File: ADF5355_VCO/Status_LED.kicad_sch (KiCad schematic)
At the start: 9 parts, among them Q1 MMBT3904, Q2 MMBT3904, Q3 MMBT3904

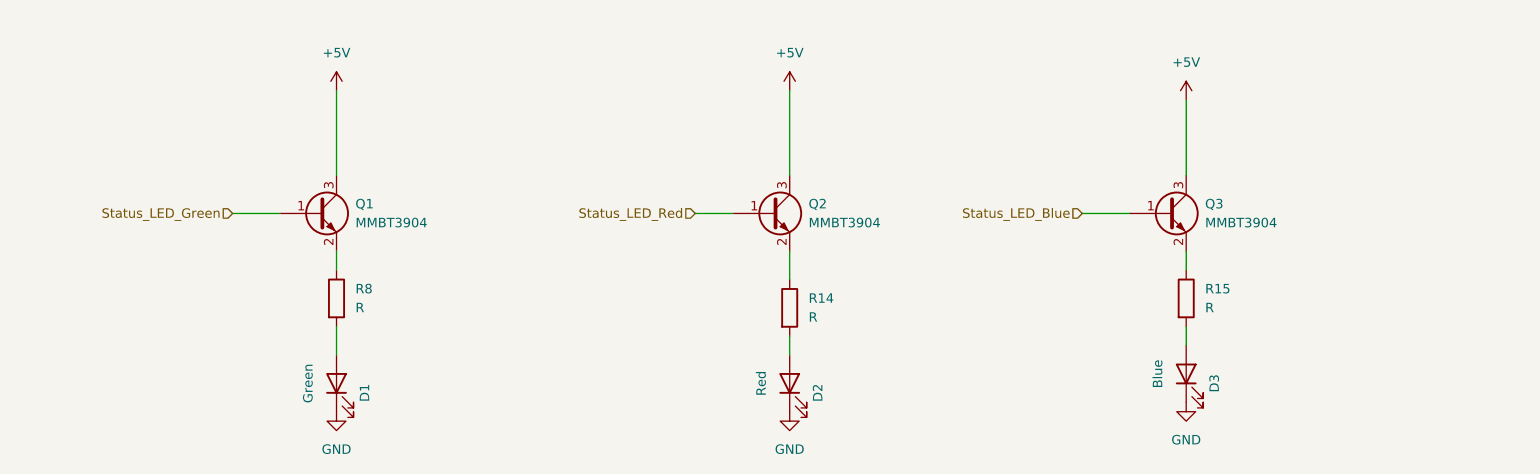
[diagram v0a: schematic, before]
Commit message: Added components for LED subsystem
Added resistor values and specific resistors and LEDs to BOM for the LED subsystem

Modified .gitignore to ignore autosave file
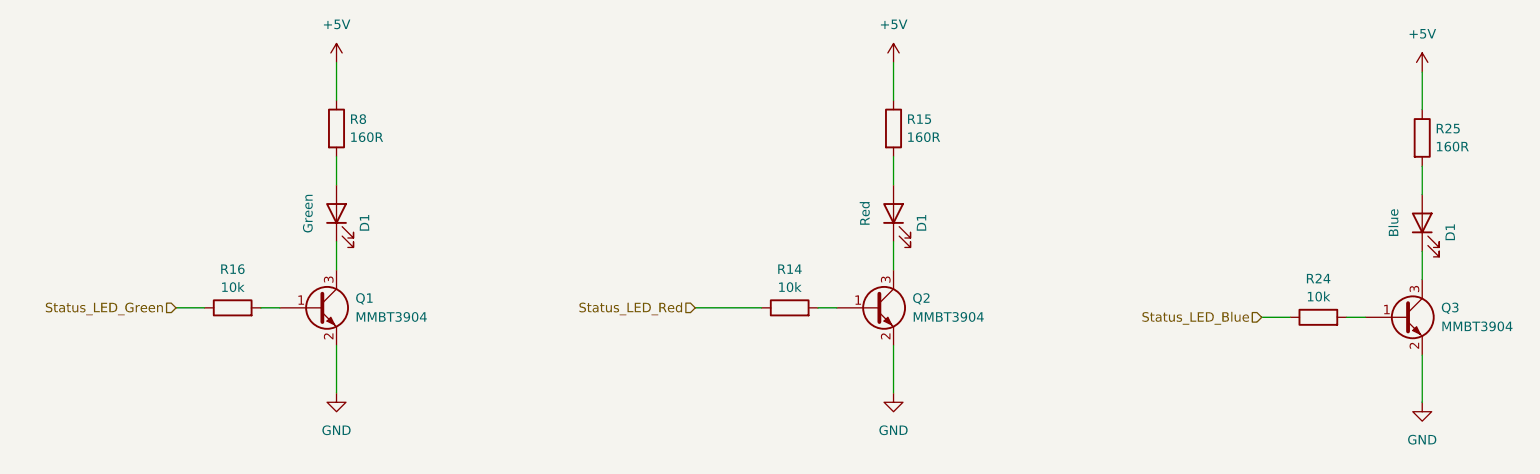
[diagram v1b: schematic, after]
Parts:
- removed D1: Green, symbol Device:LED
- removed D2: Red, symbol Device:LED
- removed D3: Blue, symbol Device:LED
- added D1: Red, LED_THT:LED_D4.0mm, symbol Device:LED
- added D1: Green, LED_THT:LED_D4.0mm, symbol Device:LED
- added D1: Blue, LED_THT:LED_D4.0mm, symbol Device:LED
- added R16, R24: 10k, Resistor_SMD:R_0603_1608Metric_Pad0.98x0.95mm_HandSolder, symbol Device:R
- added R25: 160R, Resistor_SMD:R_0603_1608Metric_Pad0.98x0.95mm_HandSolder, symbol Device:R
- R14: value R -> 10k; footprint (none) -> Resistor_SMD:R_0603_1608Metric_Pad0.98x0.95mm_HandSolder
- R15, R8: value R -> 160R; footprint (none) -> Resistor_SMD:R_0603_1608Metric_Pad0.98x0.95mm_HandSolder
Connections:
- net +5V: now also R15.1, R8.1, R25.1; no longer Q1.3 (C), Q2.3 (C), Q3.3 (C)
- net GND: now also Q1.2 (E), Q2.2 (E), Q3.2 (E)
- net Status_LED_Blue: now also R24.1; no longer Q3.1 (B)
- net Status_LED_Green: now also R16.1; no longer Q1.1 (B)
- net Status_LED_Red: now also R14.1; no longer Q2.1 (B)
- net at R8.2: now also D1.2 (A)
- net at R15.2: now also D1.2 (A)
- net at R14.2: now also Q2.1 (B)
- new net: D1.2 (A), R25.2
- new net: D1.1 (K), Q2.3 (C)
- new net: D1.1 (K), Q1.3 (C)
- new net: Q1.1 (B), R16.2
- new net: D1.1 (K), Q3.3 (C)
- new net: Q3.1 (B), R24.2
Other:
- moved on the sheet: Q1
